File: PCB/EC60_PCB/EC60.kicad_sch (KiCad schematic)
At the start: 28 parts, among them J1 JST, SW1 BOOT0, U1 STM32F401CBUx, U5 XC6206PxxxMR, Y1 8 MHz

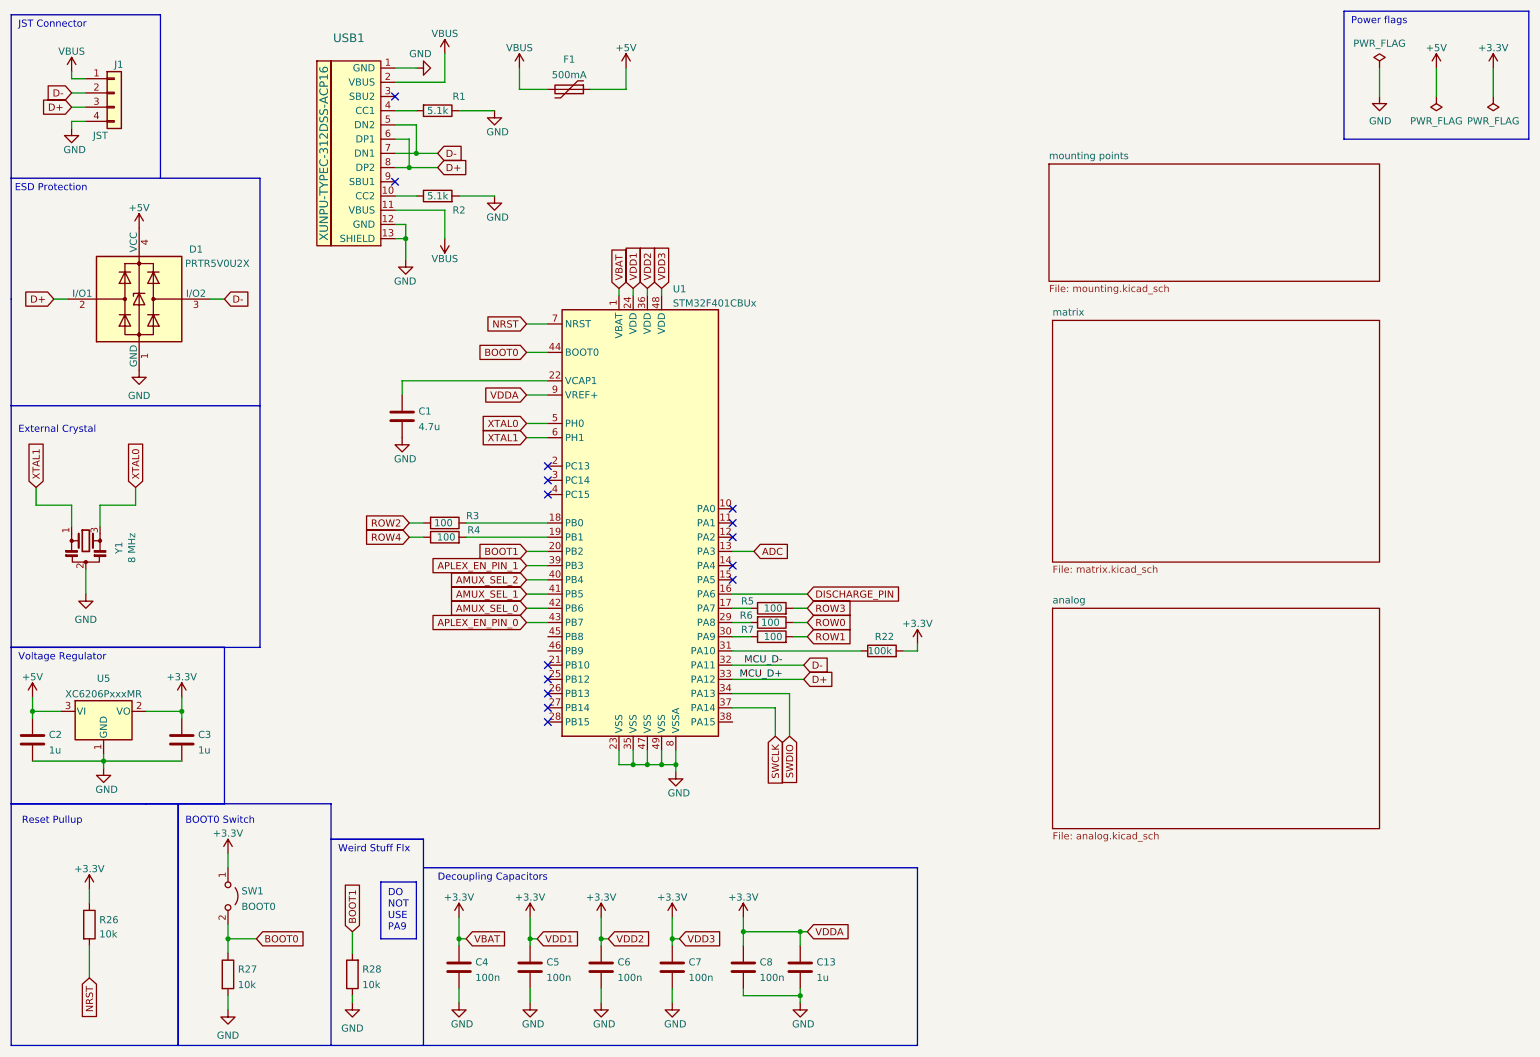
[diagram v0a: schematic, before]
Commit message: REV 1.1 upload
Some changes include:
- reassign of pins to avoid compiler problem
- changes in silkscreen
- moved to different USB port for better availability
- added 7U hhkb plate
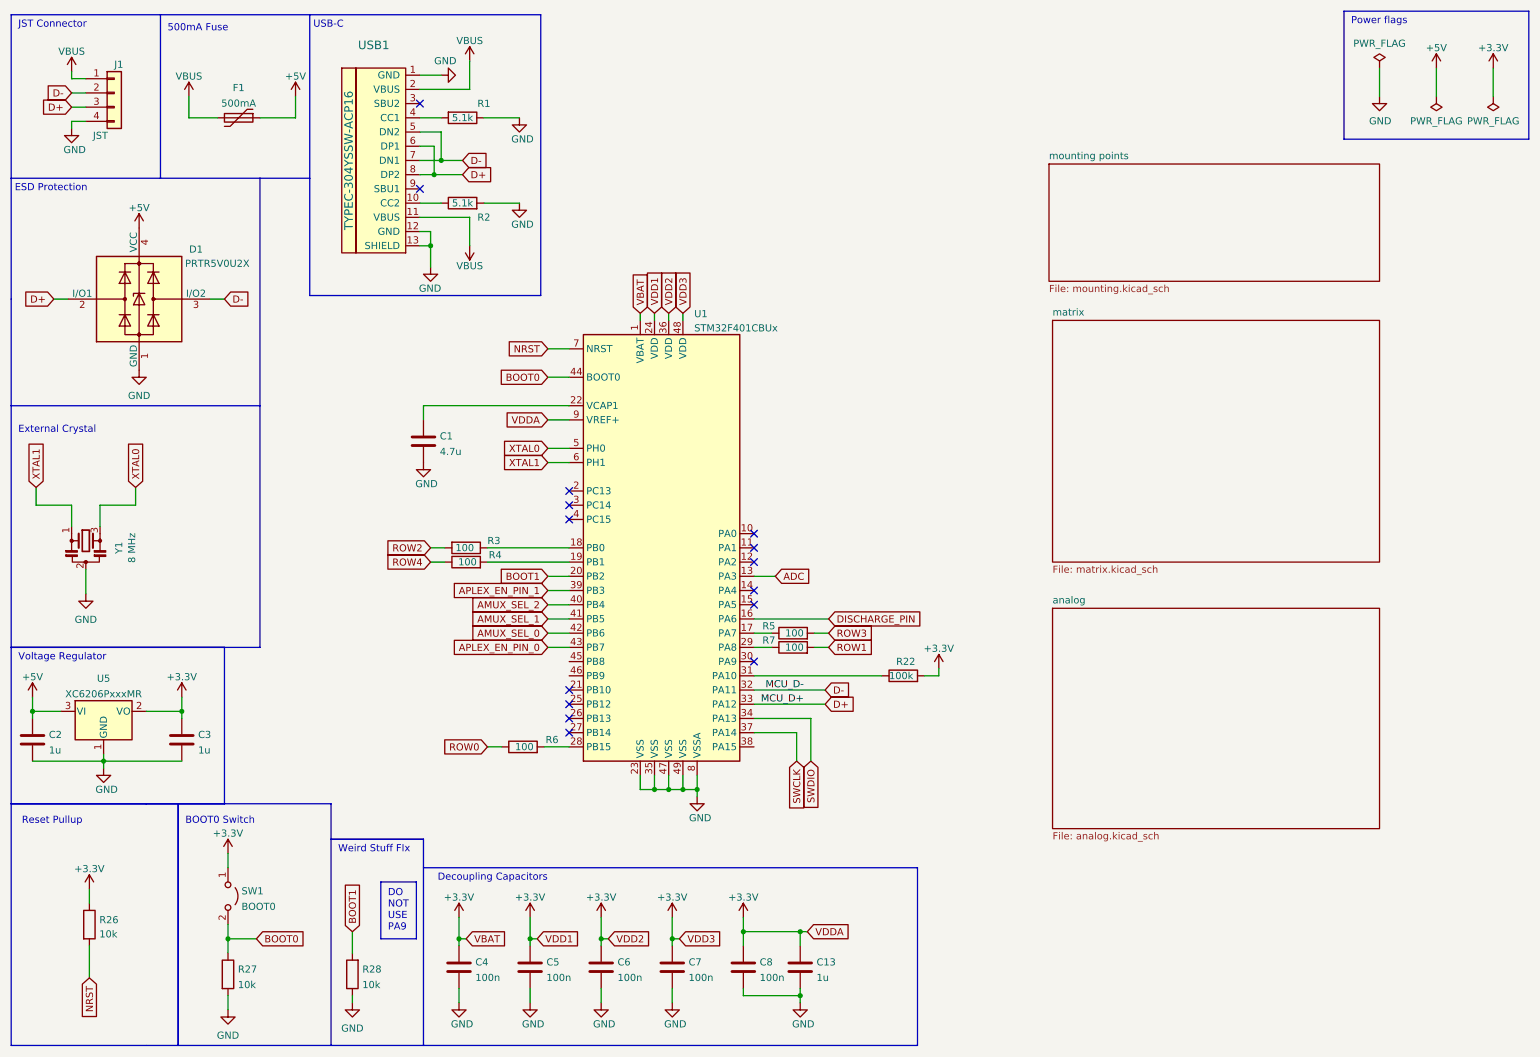
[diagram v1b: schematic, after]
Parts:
- removed USB1: XUNPU-TYPEC-312DSS-ACP16, cipulot_parts:XUNPU-TYPEC-312DSS-ACP16-Assembly, symbol cipulot_parts:XUNPU-TYPEC-312DSS-ACP16
- added USB1: TYPEC-304YSSW-ACP16, cipulot_parts:TYPEC-304YSSW-ACP16, symbol cipulot_parts:TYPEC-304YSSW-ACP16
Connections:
- net D+: now also USB1.6 (DP1), USB1.8 (DP2)
- net D-: now also USB1.5 (DN2), USB1.7 (DN1)
- net GND: now also USB1.1 (GND), USB1.12 (GND), USB1.13 (SHIELD)
- net VBUS: now also USB1.11 (VBUS), USB1.2 (VBUS)
- net at U1.28 (PB15): now also R6.2
- net at U1.29 (PA8): now also R7.1; no longer R6.2
- net at U1.30 (PA9): no longer R7.1
- net at R1.2: now also USB1.4 (CC1)
- net at R2.1: now also USB1.10 (CC2)
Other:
- note added: "500mA Fuse"
- note added: "USB-C"
- moved on the sheet: C1, F1, R1, R2, R22, R3, R4, R5, R6, R7, U1
